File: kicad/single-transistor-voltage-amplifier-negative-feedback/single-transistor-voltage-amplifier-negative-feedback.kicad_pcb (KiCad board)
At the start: 2 copper layers, 99 x 39.5 mm, 13 parts, among them J1 NMJ4HHD2, J2 NMJ4HHD2, J3 Screw_Terminal_01x02, Q1 BC337

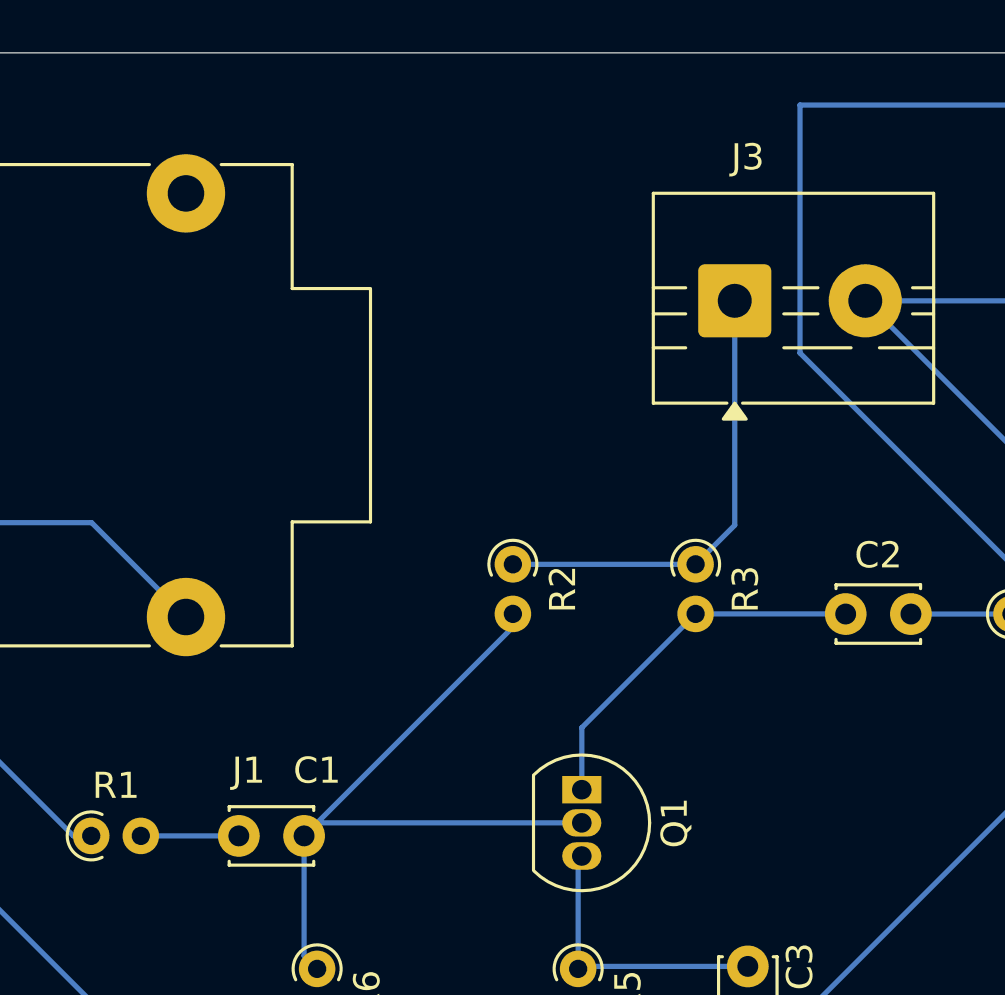
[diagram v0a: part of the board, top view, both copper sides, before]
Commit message: Add single-transistor-voltage-amplifier-negative-feedback and update readme
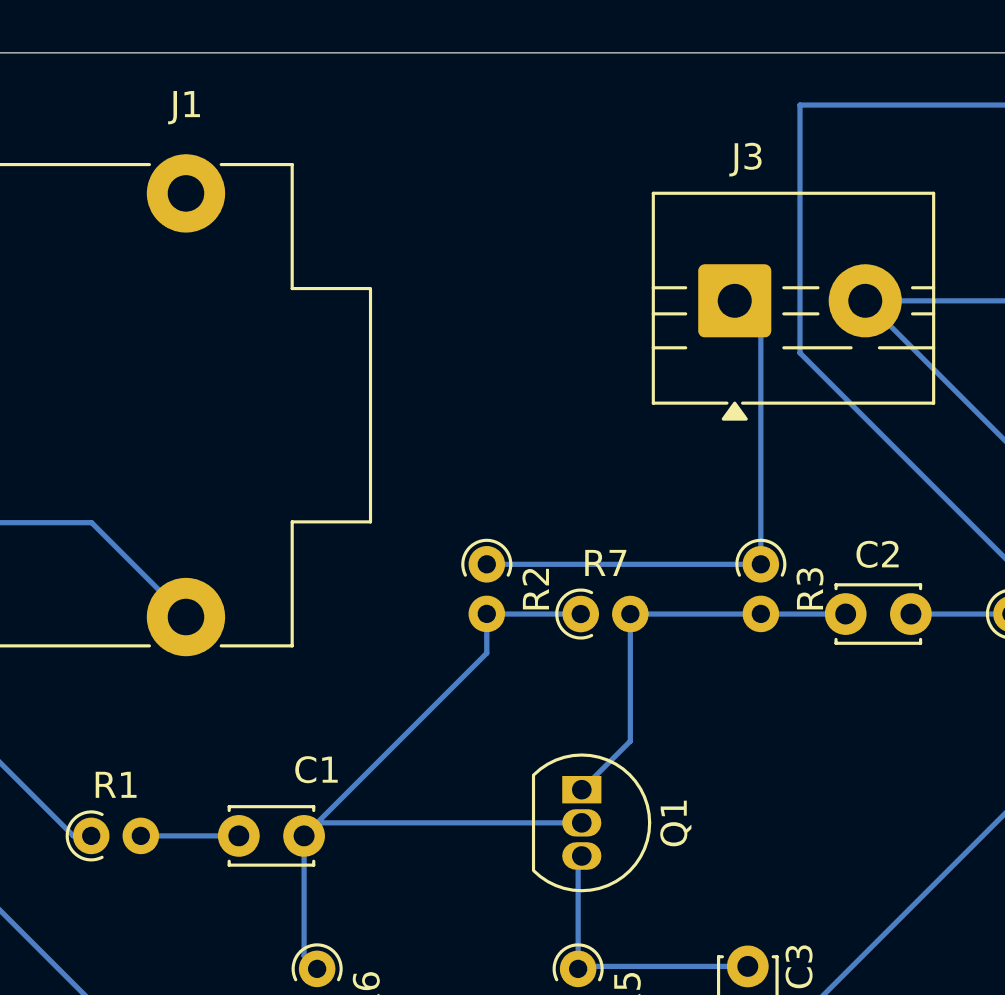
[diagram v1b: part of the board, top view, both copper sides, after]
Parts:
- added R7: 100k, Resistor_THT:R_Axial_DIN0204_L3.6mm_D1.6mm_P1.90mm_Vertical, F.Cu at (141.6, 88.0)
- R1, R3: value 4.7k -> 5.1k
- R2: value 100k -> 470k
- R4: value 3.3k -> 4.7k
- moved R3 2.50 mm to (148.5, 86.1)
- moved R2 1.00 mm to (138.0, 86.1)
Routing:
- net Net-(J3-Pin_1): track 17.7 -> 21.0 mm
- net Net-(Q1-B): track 28.0 -> 31.2 mm
- net Net-(Q1-C): track 14.3 -> 15.8 mm
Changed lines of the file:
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@@
 	(footprint "Resistor_THT:R_Axial_DIN0204_L3.6mm_D1.6mm_P1.90mm_Vertical"
 		(layer "F.Cu")
-		(at 139 86.095 -90)
+		(at 138 86.095 -90)
 		(descr "Resistor, Axial_DIN0204 series, Axial, Vertical, pin pitch=1.9mm, 0.167W, length*diameter=3.6*1.6mm^2, http://cdn-reichelt.de/documents/datenblatt/B400/1_4W%23YAG.pdf")
 		(tags "Resistor Axial_DIN0204 series Axial Vertical pin pitch 1.9mm 0.167W length 3.6mm diameter 1.6mm")
@@
 			)
 		)
-		(property "Value" "100k"
+		(property "Value" "470k"
 			(at 0.95 1.92 90)
 			(layer "F.Fab")
@@
 		(property ki_fp_filters "R_*")
 		(sheetname "/")
-		(sheetfile "single-transistor-voltage-amplifier.kicad_sch")
+		(sheetfile "single-transistor-voltage-amplifier-negative-feedback.kicad_sch")
 		(attr through_hole)
 		(fp_arc
@@
 	(footprint "Resistor_THT:R_Axial_DIN0204_L3.6mm_D1.6mm_P1.90mm_Vertical"
 		(layer "F.Cu")
-		(at 146 86.095 -90)
+		(at 148.5 86.095 -90)
 		(descr "Resistor, Axial_DIN0204 series, Axial, Vertical, pin pitch=1.9mm, 0.167W, length*diameter=3.6*1.6mm^2, http://cdn-reichelt.de/documents/datenblatt/B400/1_4W%23YAG.pdf")
 		(tags "Resistor Axial_DIN0204 series Axial Vertical pin pitch 1.9mm 0.167W length 3.6mm diameter 1.6mm")
@@
 			)
 		)
-		(property "Value" "4.7k"
+		(property "Value" "5.1k"
 			(at 0.95 1.92 90)
 			(layer "F.Fab")
@@
 		(property ki_fp_filters "R_*")
 		(sheetname "/")
-		(sheetfile "single-transistor-voltage-amplifier.kicad_sch")
+		(sheetfile "single-transistor-voltage-amplifier-negative-feedback.kicad_sch")
 		(attr through_hole)
 		(fp_arc
@@
 		(property ki_fp_filters "Jack*")
 		(sheetname "/")
-		(sheetfile "single-transistor-voltage-amplifier.kicad_sch")
+		(sheetfile "single-transistor-voltage-amplifier-negative-feedback.kicad_sch")
 		(attr through_hole)
 		(fp_line
@@
 		(property ki_fp_filters "R_*")
 		(sheetname "/")
-		(sheetfile "single-transistor-voltage-amplifier.kicad_sch")
+		(sheetfile "single-transistor-voltage-amplifier-negative-feedback.kicad_sch")
 		(attr through_hole)
 		(fp_arc
@@
 		(property ki_fp_filters "TerminalBlock*:*")
 		(sheetname "/")
-		(sheetfile "single-transistor-voltage-amplifier.kicad_sch")
+		(sheetfile "single-transistor-voltage-amplifier-negative-feedback.kicad_sch")
 		(attr through_hole)
 		(fp_line
@@
 			)
 		)
-		(property "Value" "3.3k"
+		(property "Value" "4.7k"
 			(at 0.95 1.92 0)
 			(layer "F.Fab")
@@
 		(property ki_fp_filters "R_*")
 		(sheetname "/")
-		(sheetfile "single-transistor-voltage-amplifier.kicad_sch")
+		(sheetfile "single-transistor-voltage-amplifier-negative-feedback.kicad_sch")
 		(attr through_hole)
 		(fp_arc
@@
 		(tags "neutrik jack m")
 		(property "Reference" "J1"
-			(at -2.4 -5.885 0)
+			(at -0.025 19.615 0)
 			(layer "F.SilkS")
 			(effects
@@
 		(property ki_fp_filters "Jack*")
 		(sheetname "/")
-		(sheetfile "single-transistor-voltage-amplifier.kicad_sch")
+		(sheetfile "single-transistor-voltage-amplifier-negative-feedback.kicad_sch")
 		(attr through_hole)
 		(fp_line
@@
 			)
 		)
-		(property "Value" "4.7k"
+		(property "Value" "5.1k"
 			(at 0.95 1.92 0)
 			(layer "F.Fab")
@@
 		(property ki_fp_filters "R_*")
 		(sheetname "/")
-		(sheetfile "single-transistor-voltage-amplifier.kicad_sch")
+		(sheetfile "single-transistor-voltage-amplifier-negative-feedback.kicad_sch")
 		(attr through_hole)
 		(fp_arc
@@
 		(property ki_fp_filters "R_*")
 		(sheetname "/")
-		(sheetfile "single-transistor-voltage-amplifier.kicad_sch")
+		(sheetfile "single-transistor-voltage-amplifier-negative-feedback.kicad_sch")
 		(attr through_hole)
 		(fp_arc
@@
 		(property ki_fp_filters "C_*")
 		(sheetname "/")
-		(sheetfile "single-transistor-voltage-amplifier.kicad_sch")
+		(sheetfile "single-transistor-voltage-amplifier-negative-feedback.kicad_sch")
 		(attr through_hole)
 		(fp_line
@@
 		(property ki_fp_filters "C_*")
 		(sheetname "/")
-		(sheetfile "single-transistor-voltage-amplifier.kicad_sch")
+		(sheetfile "single-transistor-voltage-amplifier-negative-feedback.kicad_sch")
 		(attr through_hole)
 		(fp_line
@@
 		(property ki_fp_filters "C_*")
 		(sheetname "/")
-		(sheetfile "single-transistor-voltage-amplifier.kicad_sch")
+		(sheetfile "single-transistor-voltage-amplifier-negative-feedback.kicad_sch")
 		(attr through_hole)
 		(fp_line
@@
 		(property ki_fp_filters "TO?92*")
 		(sheetname "/")
-		(sheetfile "single-transistor-voltage-amplifier.kicad_sch")
+		(sheetfile "single-transistor-voltage-amplifier-negative-feedback.kicad_sch")
 		(attr through_hole)
 		(fp_line
@@
 		)
 	)
+	(footprint "Resistor_THT:R_Axial_DIN0204_L3.6mm_D1.6mm_P1.90mm_Vertical"
+		(layer "F.Cu")
+		(at 141.6 88)
+		(descr "Resistor, Axial_DIN0204 series, Axial, Vertical, pin pitch=1.9mm, 0.167W, length*diameter=3.6*1.6mm^2, http://cdn-reichelt.de/documents/datenblatt/B400/1_4W%23YAG.pdf")
+		(tags "Resistor Axial_DIN0204 series Axial Vertical pin pitch 1.9mm 0.167W length 3.6mm diameter 1.6mm")
+		(property "Reference" "R7"
+			(at 0.95 -1.92 0)
+			(layer "F.SilkS")
+			(effects
+				(font
+					(size 1 1)
+					(thickness 0.15)
+				)
+			)
+		)
+		(property "Value" "100k"
+			(at 0.95 1.92 0)
+			(layer "F.Fab")
+			(effects
+				(font
+					(size 1 1)
+					(thickness 0.15)
+				)
+			)
+		)
+		(property "Datasheet" "~"
+			(at 0 0 0)
+			(layer "F.Fab")
+			(hide yes)
+			(effects
+				(font
+					(size 1.27 1.27)
+					(thickness 0.15)
+				)
+			)
+		)
+		(property "Description" "Resistor"
+			(at 0 0 0)
+			(layer "F.Fab")
+			(hide yes)
+			(effects
+				(font
+					(size 1.27 1.27)
+					(thickness 0.15)
+				)
+			)
+		)
+		(property ki_fp_filters "R_*")
+		(sheetname "/")
+		(sheetfile "single-transistor-voltage-amplifier-negative-feedback.kicad_sch")
+		(attr through_hole)
+		(fp_arc
+			(start 0.417133 0.82)
+			(mid -0.92 0)
+			(end 0.417133 -0.82)
+			(stroke
+				(width 0.12)
+				(type solid)
+			)
+			(layer "F.SilkS")
+		)
+		(fp_rect
+			(start -1.05 -1.05)
+			(end 2.86 1.05)
+			(stroke
+				(width 0.05)
+				(type solid)
+			)
+			(fill no)
+			(layer "F.CrtYd")
+		)
+		(fp_line
+			(start 0 0)
+			(end 1.9 0)
+			(stroke
+				(width 0.1)
+				(type solid)
+			)
+			(layer "F.Fab")
+		)
+		(fp_circle
+			(center 0 0)
+			(end 0.8 0)
+			(stroke
+				(width 0.1)
+				(type solid)
+			)
+			(fill no)
+			(layer "F.Fab")
+		)
+		(fp_text user "${REFERENCE}"
+			(at 0.95 -1.92 0)
+			(layer "F.Fab")
+			(effects
+				(font
+					(size 1 1)
+					(thickness 0.15)
+				)
+			)
+		)
+		(pad "1" thru_hole circle
+			(at 0 0)
+			(size 1.4 1.4)
+			(drill 0.7)
+			(layers "*.Cu" "*.Mask")
+			(remove_unused_layers no)
+			(net 2 "Net-(Q1-B)")
+			(pintype "passive")
+		)
+		(pad "2" thru_hole circle
+			(at 1.9 0)
+			(size 1.4 1.4)
+			(drill 0.7)
+			(layers "*.Cu" "*.Mask")
+			(remove_unused_layers no)
+			(net 3 "Net-(Q1-C)")
+			(pintype "passive")
+		)
+		(embedded_fonts no)
+		(model "${KICAD9_3DMODEL_DIR}/Resistor_THT.3dshapes/R_Axial_DIN0204_L3.6mm_D1.6mm_P1.90mm_Vertical.step"
+			(offset
+				(xyz 0 0 0)
+			)
+			(scale
+				(xyz 1 1 1)
+			)
+			(rotate
+				(xyz 0 0 0)
+			)
+		)
+	)
 	(gr_rect
 		(start 99.5 66.5)
@@
 	)
 	(segment
+		(start 138.005 88)
+		(end 138 87.995)
+		(width 0.2)
+		(layer "B.Cu")
+		(net 2)
+	)
+	(segment
+		(start 141.6 88)
+		(end 138.005 88)
+		(width 0.2)
+		(layer "B.Cu")
+		(net 2)
+	)
+	(segment
 		(start 131 96.5)
 		(end 131 101.095)
@@
 	)
 	(segment
-		(start 139 88.5)
-		(end 139 87.995)
+		(start 138 89.5)
+		(end 131 96.5)
 		(width 0.2)
 		(layer "B.Cu")
@@
 	)
 	(segment
-		(start 131 96.5)
-		(end 139 88.5)
+		(start 138 87.995)
+		(end 138 89.5)
 		(width 0.2)
 		(layer "B.Cu")
@@
 	)
 	(segment
-		(start 141.64 94.73)
-		(end 141.64 92.355)
+		(start 143.5 88)
+		(end 143.5 92.87)
+		(width 0.2)
+		(layer "B.Cu")
+		(net 3)
+	)
+	(segment
+		(start 143.5 92.87)
+		(end 141.64 94.73)
+		(width 0.2)
+		(layer "B.Cu")
+		(net 3)
+	)
+	(segment
+		(start 151.75 88)
+		(end 148.505 88)
+		(width 0.2)
+		(layer "B.Cu")
+		(net 3)
+	)
+	(segment
+		(start 148.495 88)
+		(end 148.5 87.995)
 		(width 0.2)
 		(layer "B.Cu")
@@
 	)
 	(segment
-		(start 146 87.995)
-		(end 151.745 87.995)
+		(start 148.505 88)
+		(end 148.5 87.995)
 		(width 0.2)
 		(layer "B.Cu")
@@
 	)
 	(segment
-		(start 141.64 92.355)
-		(end 146 87.995)
+		(start 143.5 88)
+		(end 148.495 88)
 		(width 0.2)
 		(layer "B.Cu")
@@
 	)
 	(segment
-		(start 139 86.095)
-		(end 146 86.095)
+		(start 148.5 86.095)
+		(end 148.5 77)
 		(width 0.2)
 		(layer "B.Cu")
@@
 	)
 	(segment
-		(start 147.5 76)
-		(end 147.5 84.595)
+		(start 148.5 77)
+		(end 147.5 76)
 		(width 0.2)
 		(layer "B.Cu")
@@
 	)
 	(segment
-		(start 147.5 84.595)
-		(end 146 86.095)
+		(start 138 86.095)
+		(end 148.5 86.095)
 		(width 0.2)
 		(layer "B.Cu")
